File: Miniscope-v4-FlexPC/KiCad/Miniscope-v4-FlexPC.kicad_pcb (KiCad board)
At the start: 2 copper layers, 7.2 x 10.4 mm, 2 parts, among them J1 Conn_01x20, J2 Conn_01x20

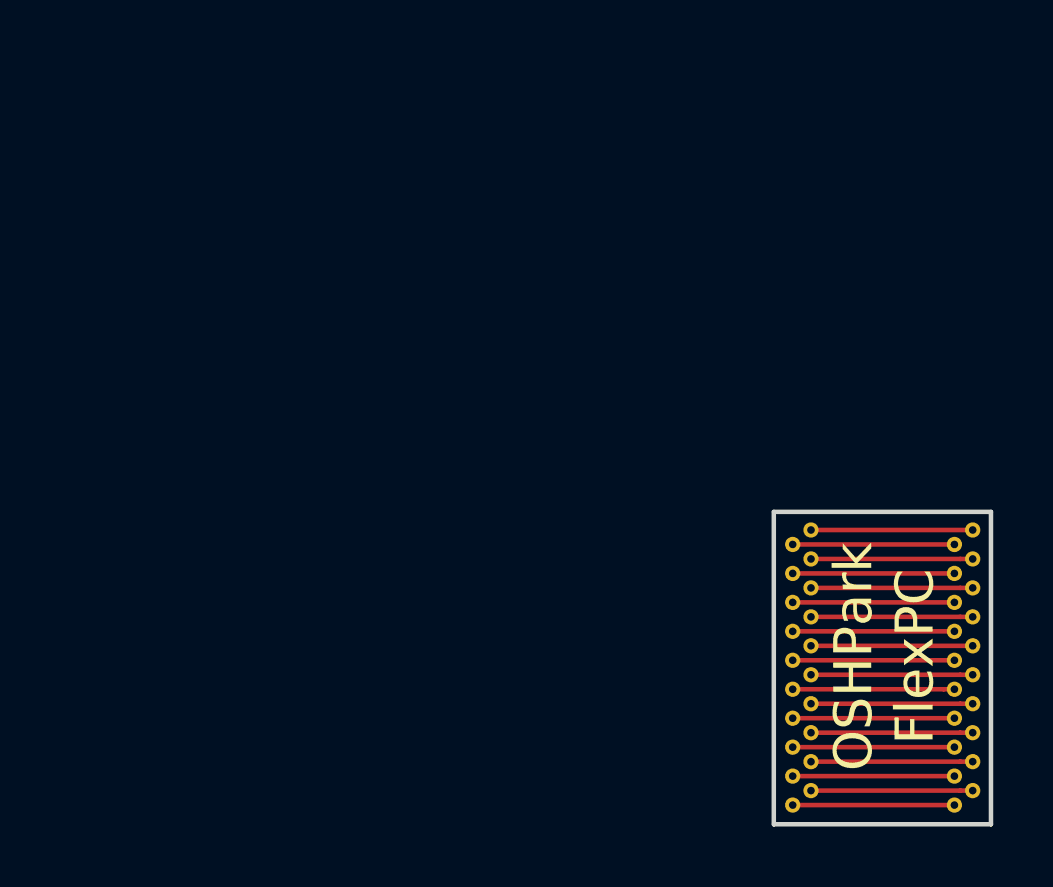
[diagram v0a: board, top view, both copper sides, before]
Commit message: Combine Miniscope-v4-SER-POW
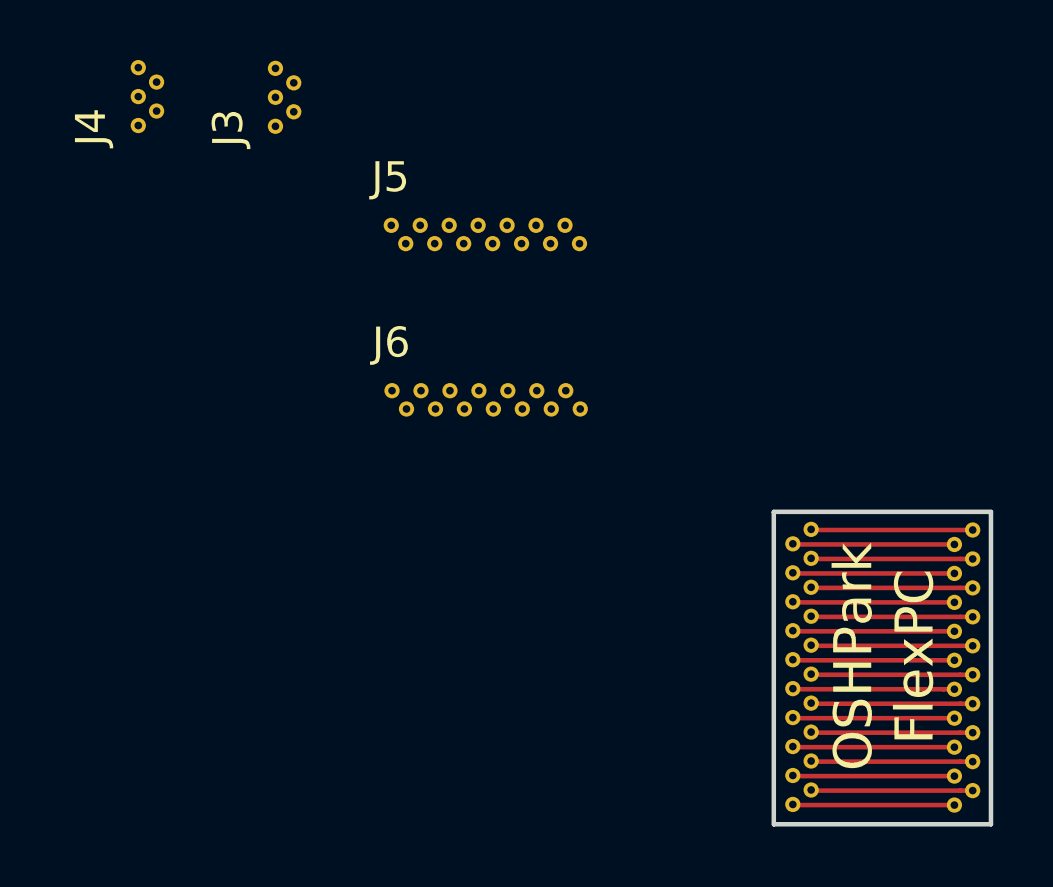
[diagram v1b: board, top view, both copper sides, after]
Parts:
- added J3: Conn_01x05, .Connector:B2B_Flex_05_Dual_Row_38milx24mil_Hole_20mil, F.Cu at (22.8, 17.4)
- added J4: Conn_01x05, .Connector:B2B_Flex_05_Dual_Row_38milx24mil_Hole_20mil, F.Cu at (18.2, 17.4)
- added J5: Conn_01x14, .Connector:B2B_Flex_14_Dual_Row_38milx24mil_Hole_10milx20mil, F.Cu at (26.6, 20.7)
- added J6: Conn_01x14, .Connector:B2B_Flex_14_Dual_Row_38milx24mil_Hole_10milx20mil, F.Cu at (26.6, 26.2)
- moved J2 9.21 mm to (40.6, 30.8), turned to 270 degrees
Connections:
- J2 pad 1: Net-(J1-Pad20) -> Net-(J1-Pad1)
- J2 pad 10: Net-(J1-Pad11) -> Net-(J1-Pad10)
- J2 pad 11: Net-(J1-Pad10) -> Net-(J1-Pad11)
- J2 pad 12: Net-(J1-Pad9) -> Net-(J1-Pad12)
- J2 pad 13: Net-(J1-Pad8) -> Net-(J1-Pad13)
- J2 pad 14: Net-(J1-Pad7) -> Net-(J1-Pad14)
- J2 pad 15: Net-(J1-Pad6) -> Net-(J1-Pad15)
- J2 pad 16: Net-(J1-Pad5) -> Net-(J1-Pad16)
- J2 pad 17: Net-(J1-Pad4) -> Net-(J1-Pad17)
- J2 pad 18: Net-(J1-Pad3) -> Net-(J1-Pad18)
- J2 pad 19: Net-(J1-Pad2) -> Net-(J1-Pad19)
- J2 pad 2: Net-(J1-Pad19) -> Net-(J1-Pad2)
- J2 pad 20: Net-(J1-Pad1) -> Net-(J1-Pad20)
- J2 pad 3: Net-(J1-Pad18) -> Net-(J1-Pad3)
- J2 pad 4: Net-(J1-Pad17) -> Net-(J1-Pad4)
- J2 pad 5: Net-(J1-Pad16) -> Net-(J1-Pad5)
- J2 pad 6: Net-(J1-Pad15) -> Net-(J1-Pad6)
- J2 pad 7: Net-(J1-Pad14) -> Net-(J1-Pad7)
- J2 pad 8: Net-(J1-Pad13) -> Net-(J1-Pad8)
- J2 pad 9: Net-(J1-Pad12) -> Net-(J1-Pad9)
